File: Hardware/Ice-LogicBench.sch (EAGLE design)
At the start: 106 parts, among them IC1 S27KL0641DABHV020, IC2 S26KL128SDABHI020, IC3 USBLC6-2SC6, IC4 ICE40HX4K-BG121, IC5 FUSB302MPX, IC6 USBLC6-2SC6, J2 QWIIC_RIGHT_ANGLE, Y3 12MZ

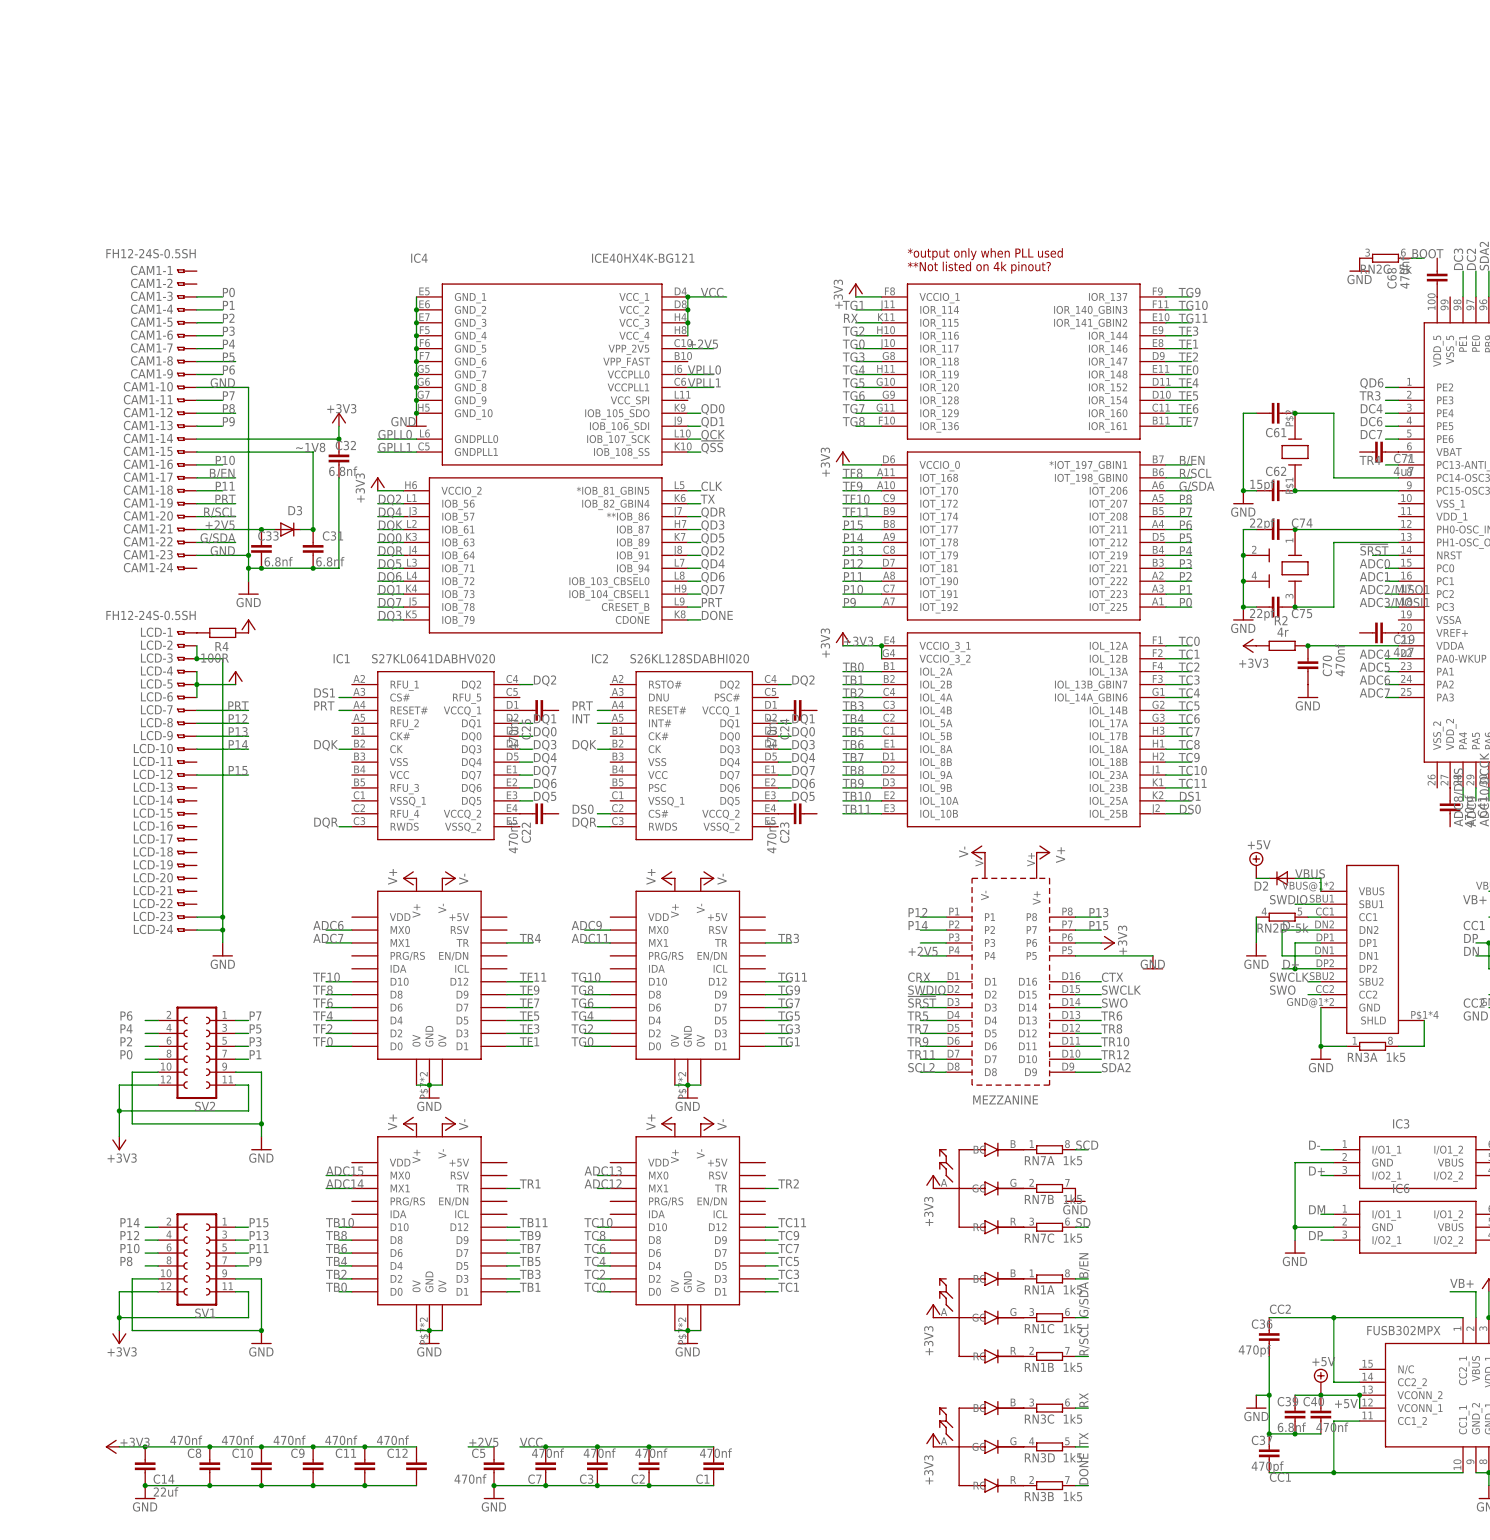
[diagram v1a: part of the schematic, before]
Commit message: Added series resistors for fast data lines and a cs jumper to alloy hyperflash to be swapped by 2nd hyperram
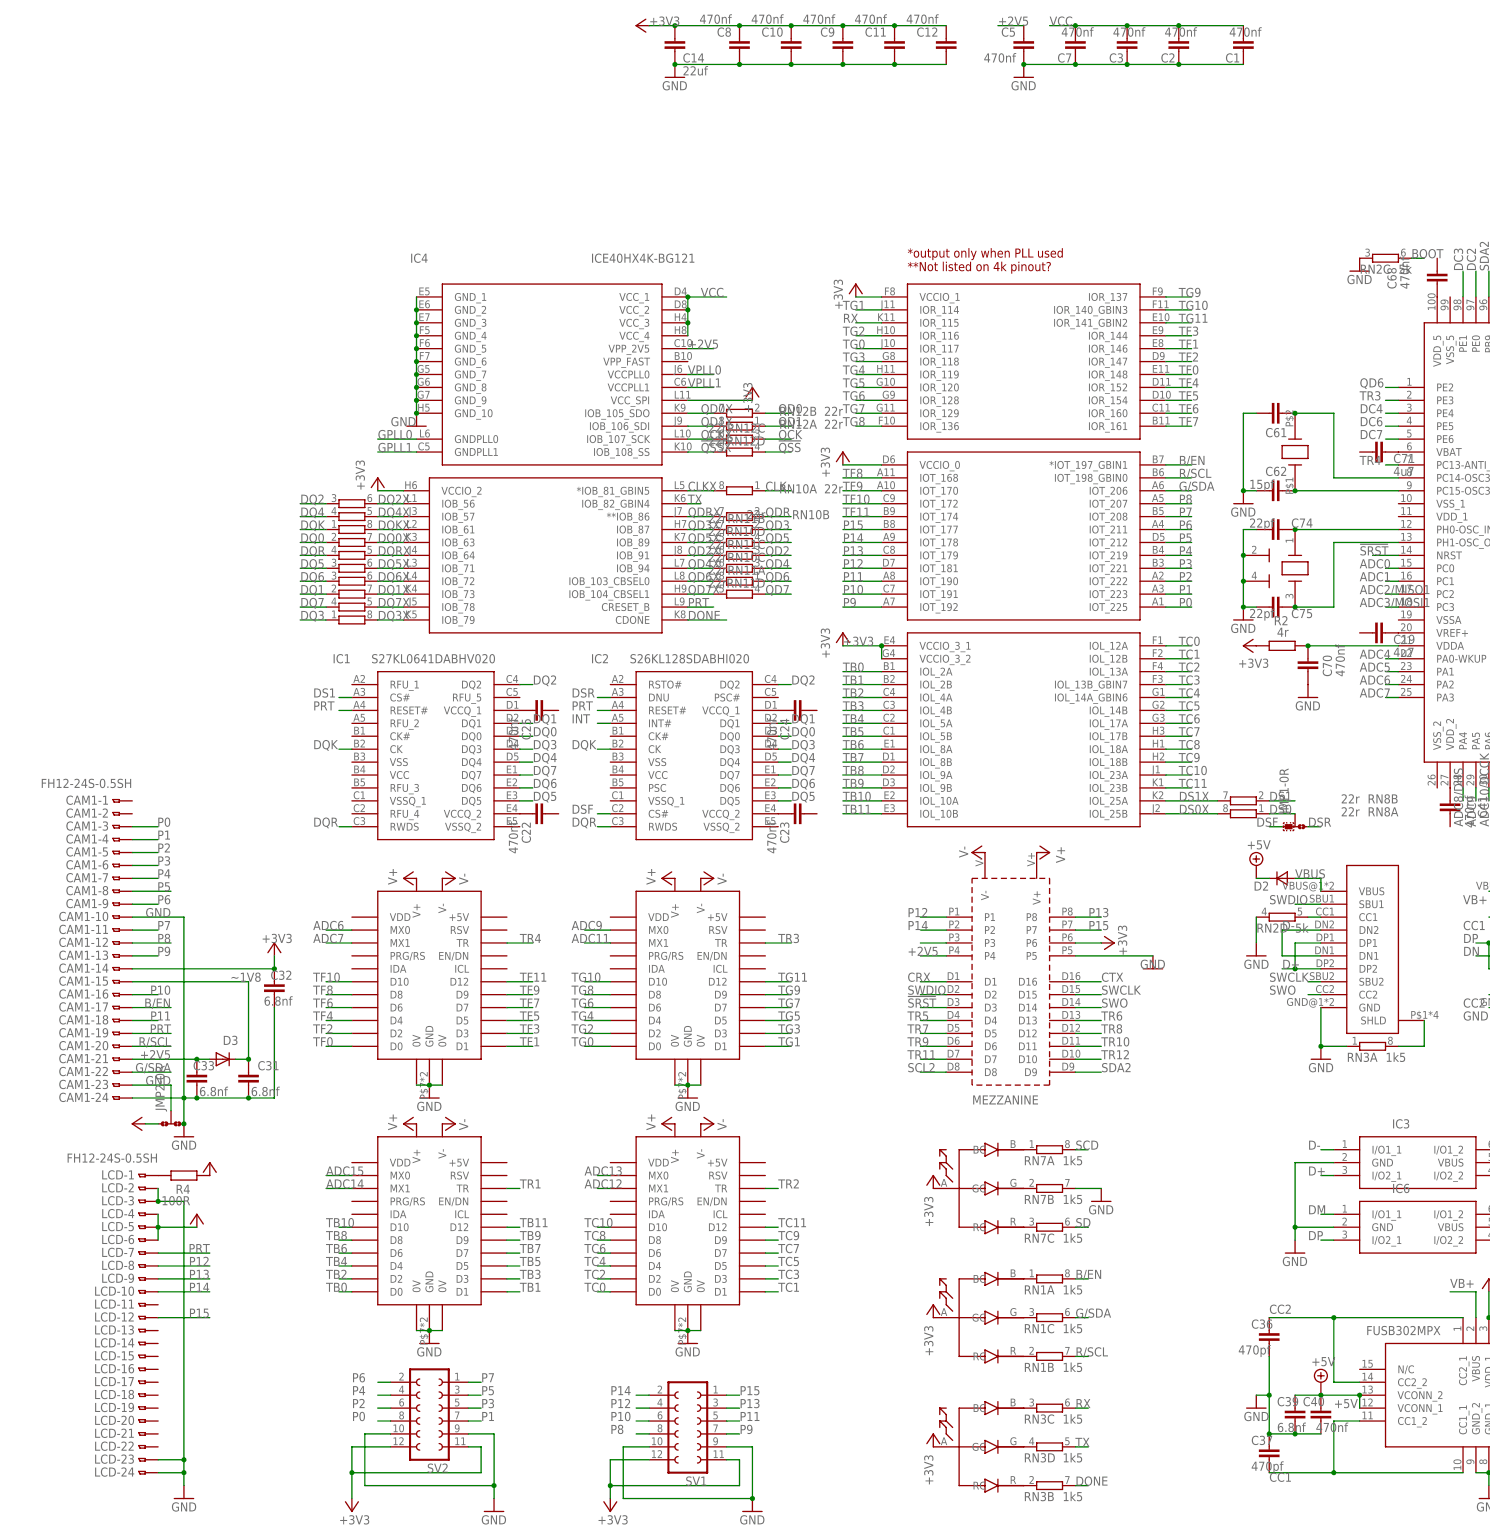
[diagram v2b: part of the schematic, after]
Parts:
- added JMP1, JMP2: 0R-JUMPC, jump-0r-smd:0R-JUMPC
- added RN10, RN11, RN12, RN6, RN8, RN9: 22r, resistor-dil:4R-NEXB38V
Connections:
- new net !QSSX: IC4.IOB_108_SS, RN12D.2
- new net CLKX: IC4.*IOB_81_GBIN5, RN10A.2
- new net DQ0X: IC4.IOB_63, RN6B.2
- new net DQ1X: IC4.IOB_73, RN9B.2
- new net DQ2X: IC4.IOB_56, RN8C.2
- new net DQ3X: IC4.IOB_79, RN9A.2
- new net DQ4X: IC4.IOB_57, RN8D.2
- new net DQ5X: IC4.IOB_71, RN6C.2
- new net DQ6X: IC4.IOB_72, RN9C.2
- new net DQ7X: IC4.IOB_78, RN9D.2
- new net DQKX: IC4.IOB_61, RN6A.2
- new net DQRX: IC4.IOB_64, RN6D.2
- new net DS0X: IC4.IOL_25B, RN8A.2
- new net DS1X: IC4.IOL_25A, RN8B.2
- new net DSF: IC2.CS#, JMP1-0R.1
- new net DSR: IC2.DNU, JMP1-0R.3
- new net N$26: CAM1-23.1, JMP2-0R.2
- new net QCKX: IC4.IOB_107_SCK, RN12C.2
- new net QD0X: IC4.IOB_105_SDO, RN12B.2
- new net QD1X: IC4.IOB_106_SDI, RN12A.2
- new net QD2X: IC4.IOB_91, RN11C.2
- new net QD3X: IC4.IOB_87, RN11B.2
- new net QD4X: IC4.IOB_94, RN10C.2
- new net QD5X: IC4.IOB_89, RN10D.2
- new net QD6X: IC4.IOB_103_CBSEL0, RN11A.2
- new net QD7X: IC4.IOB_104_CBSEL1, RN11D.2
- new net QDRX: IC4.**IOB_86, RN10B.2
- net !QSS: now also RN12D.1; no longer IC4.IOB_108_SS
- net +3V3: now also IC4.VCC_SPI, JMP2-0R.1
- net CLK: now also RN10A.1; no longer IC4.*IOB_81_GBIN5
- net DQ0: now also RN6B.1; no longer IC4.IOB_63
- net DQ1: now also RN9B.1; no longer IC4.IOB_73
- net DQ2: now also RN8C.1; no longer IC4.IOB_56
- net DQ3: now also RN9A.1; no longer IC4.IOB_79
- net DQ4: now also RN8D.1; no longer IC4.IOB_57
- net DQ5: now also RN6C.1; no longer IC4.IOB_71
- net DQ6: now also RN9C.1; no longer IC4.IOB_72
- net DQ7: now also RN9D.1; no longer IC4.IOB_78
- net DQK: now also RN6A.1; no longer IC4.IOB_61
- net DQR: now also RN6D.1; no longer IC4.IOB_64
- net DS0: now also JMP1-0R.2, RN8A.1; no longer IC2.CS#, IC4.IOL_25B
- net DS1: now also RN8B.1; no longer IC4.IOL_25A
- net GND: now also CAM1-24.1, JMP2-0R.3; no longer CAM1-23.1
- net QCK: now also RN12C.1; no longer IC4.IOB_107_SCK
- net QD0: now also RN12B.1; no longer IC4.IOB_105_SDO
- net QD1: now also RN12A.1; no longer IC4.IOB_106_SDI
- net QD2: now also RN11C.1; no longer IC4.IOB_91
- net QD3: now also RN11B.1; no longer IC4.IOB_87
- net QD4: now also RN10C.1; no longer IC4.IOB_94
- net QD5: now also RN10D.1; no longer IC4.IOB_89
- net QD6: now also RN11A.1; no longer IC4.IOB_103_CBSEL0
- net QD7: now also RN11D.1; no longer IC4.IOB_104_CBSEL1
- net QDR: now also RN10B.1; no longer IC4.**IOB_86
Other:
- moved on the sheet: C1, C10, C11, C12, C14, C2, C3, C31, C32, C33, C5, C7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
